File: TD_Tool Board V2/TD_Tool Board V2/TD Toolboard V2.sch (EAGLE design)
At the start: 138 parts, among them J3 JST-MICROFIT, M1 NMOSFET_WSD3066DN33, M2 CJ3400, M3 CJ3400, M4 CJ3400, P1 TPS54202_BUCKCONV, P2 3.3V, U1 RP2040, U2 W25Q128, U3 SN65HVD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

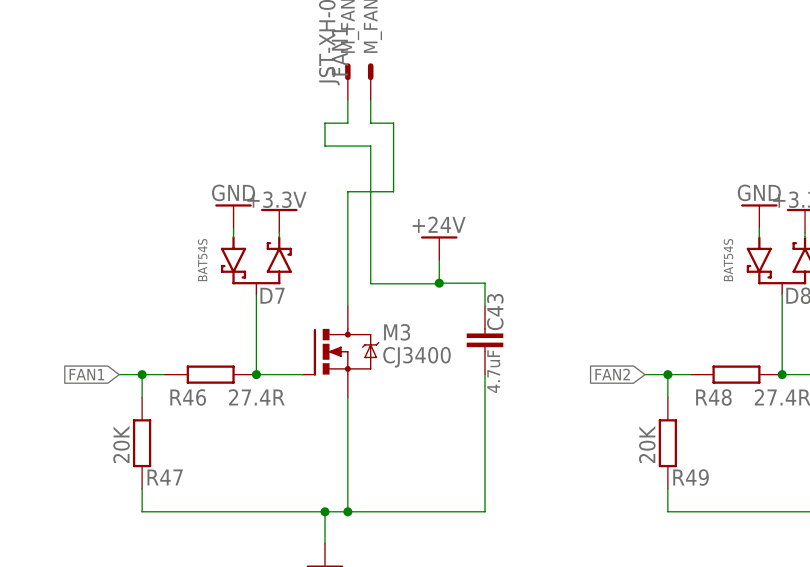
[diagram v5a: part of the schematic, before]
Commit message: routed the connections for the connectors whose logic were changed
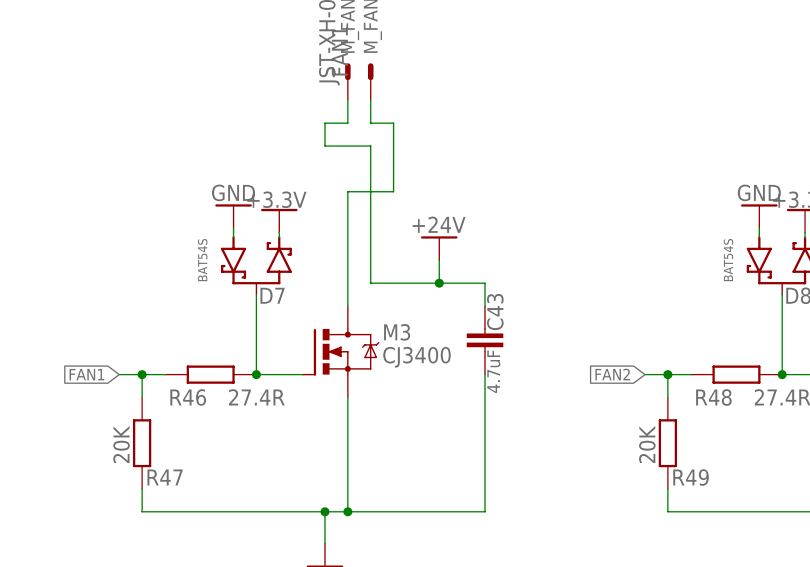
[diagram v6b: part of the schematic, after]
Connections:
- removed net N$2: M_FAN-1.S
- net +24V: now also M_FAN-1.S
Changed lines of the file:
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@@
 </segment>
 <segment>
-<wire x1="436.88" y1="-363.29" x2="444.5" y2="-363.29" width="0.1524" layer="91"/>
 <wire x1="444.5" y1="-363.29" x2="444.5" y2="-363.22" width="0.1524" layer="91"/>
 <pinref part="SUPPLY91" gate="G$1" pin="+12V"/>
@@
 <pinref part="C43" gate="G$1" pin="1"/>
 <junction x="444.5" y="-363.22"/>
+<wire x1="436.88" y1="-363.22" x2="436.88" y2="-347.98" width="0.1524" layer="91"/>
+<wire x1="436.88" y1="-347.98" x2="431.8" y2="-347.98" width="0.1524" layer="91"/>
+<wire x1="431.8" y1="-347.98" x2="431.8" y2="-345.44" width="0.1524" layer="91"/>
+<wire x1="431.8" y1="-345.44" x2="434.34" y2="-345.44" width="0.1524" layer="91"/>
+<pinref part="M_FAN" gate="-1" pin="S"/>
+<wire x1="434.34" y1="-345.44" x2="434.34" y2="-342.9" width="0.1524" layer="91"/>
+<wire x1="436.88" y1="-363.22" x2="444.5" y2="-363.22" width="0.1524" layer="91"/>
 </segment>
 <segment>
@@
 </segment>
 </net>
-<net name="N$2" class="0">
-<segment>
-<wire x1="436.88" y1="-363.22" x2="436.88" y2="-347.98" width="0.1524" layer="91"/>
-<wire x1="436.88" y1="-347.98" x2="431.8" y2="-347.98" width="0.1524" layer="91"/>
-<wire x1="431.8" y1="-347.98" x2="431.8" y2="-345.44" width="0.1524" layer="91"/>
-<wire x1="431.8" y1="-345.44" x2="434.34" y2="-345.44" width="0.1524" layer="91"/>
-<pinref part="M_FAN" gate="-1" pin="S"/>
-<wire x1="434.34" y1="-345.44" x2="434.34" y2="-342.9" width="0.1524" layer="91"/>
-</segment>
-</net>

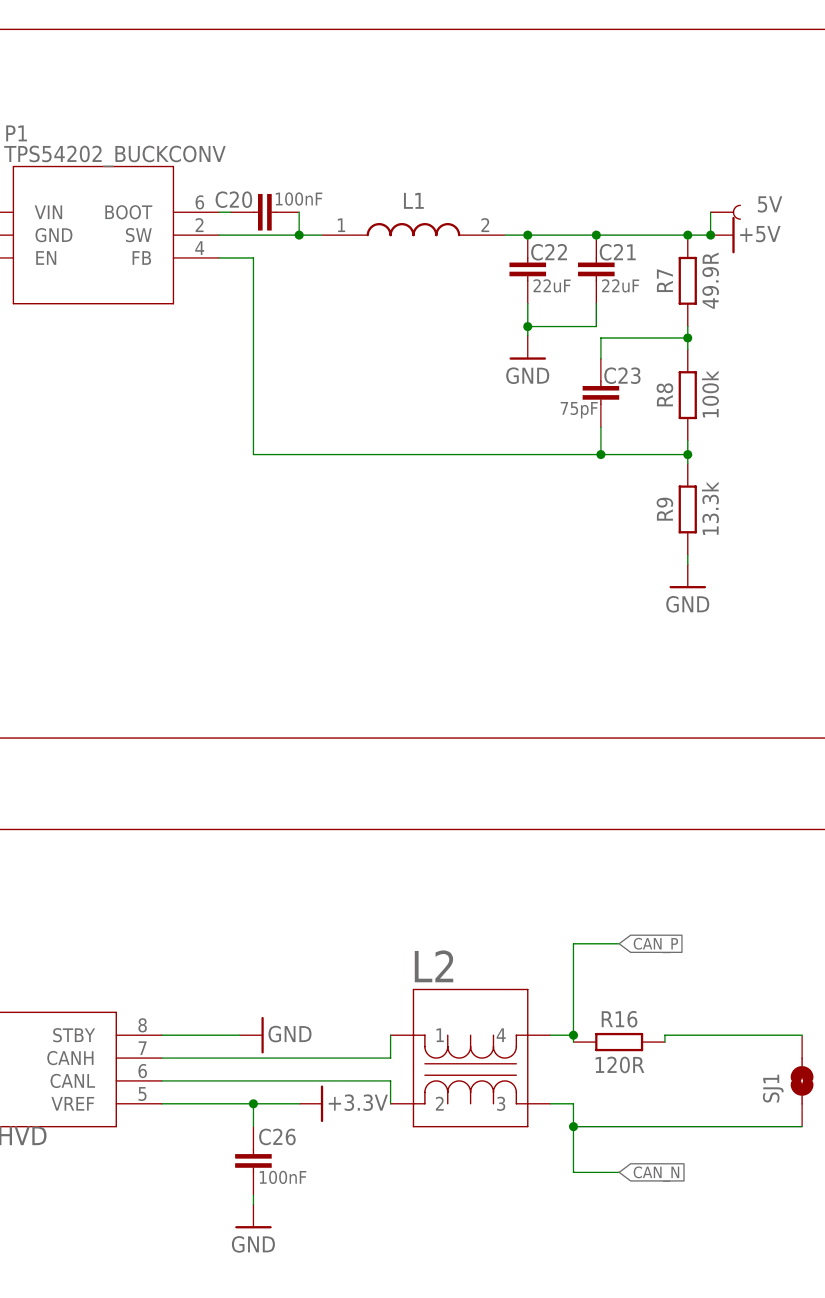
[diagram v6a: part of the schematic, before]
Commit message: Updated Toolboard V2 and Carriage minifit boards specs
Toolboard and Carriage minifit board design,  gerber, BOMs, centroids and connector specifications have been updated here
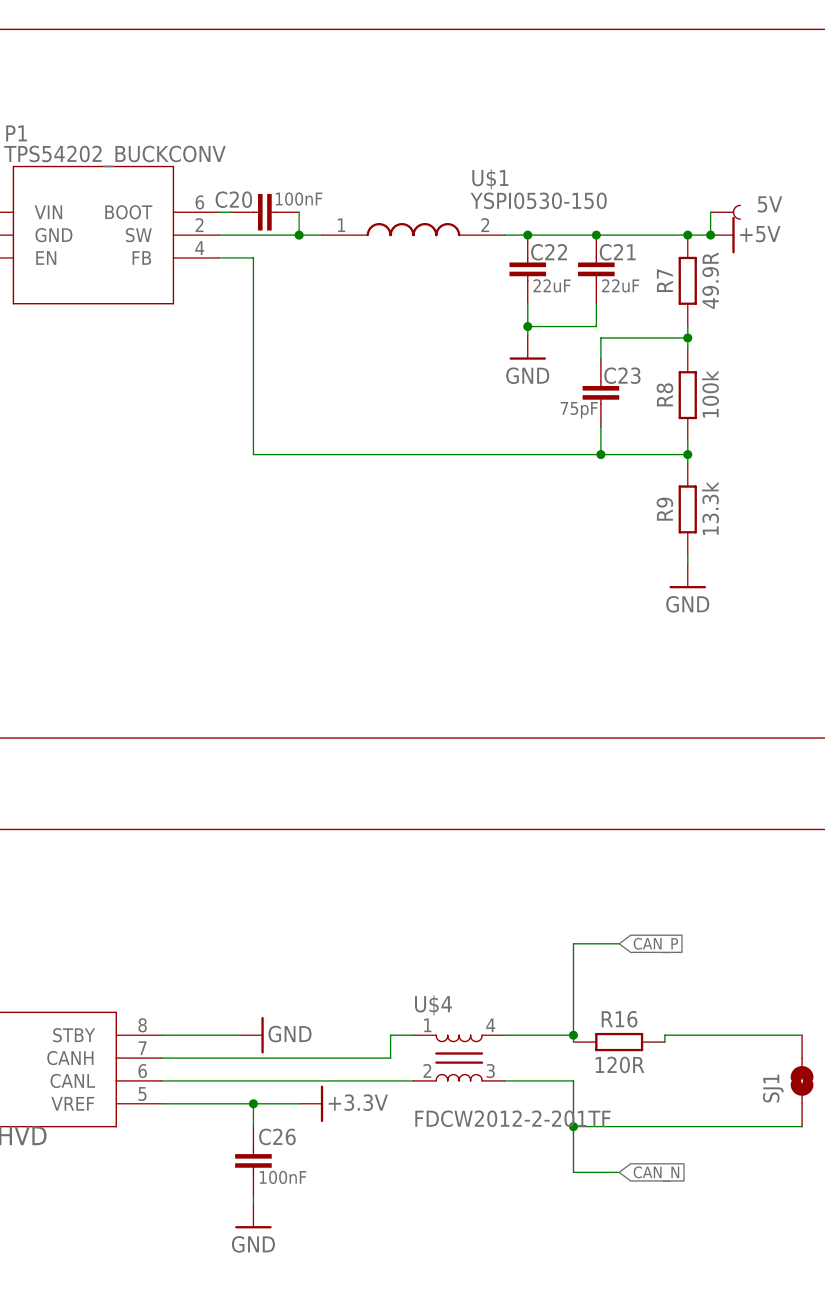
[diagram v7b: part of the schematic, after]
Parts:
- removed L1: ASPI-0630HI-100M-T157X7X4, Fracktal Misc Lib:ASPI-0630HI-100M-T157X7X4
- removed L2: ACM2012, 2023-04-02_14-21-16_Library:ACM2012-201-2P-T002ACM2012_TDK
- added U$1: YSPI0530-150, Fracktal_Dragon_ToolBoard_Components:YSPI0530-150
- added U$4: FDCW2012-2-201TF, Fracktal_Dragon_ToolBoard_Components:FDCW2012-2-201TF
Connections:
- net +5V: now also U$1.2; no longer L1.2
- net CAN1_N: now also U$4.2; no longer L2.2
- net CAN1_P: now also U$4.1; no longer L2.1
- net CAN_N: now also U$4.3; no longer L2.3
- net CAN_P: now also U$4.4; no longer L2.4
- net VREGO: now also U$1.1; no longer L1.1
